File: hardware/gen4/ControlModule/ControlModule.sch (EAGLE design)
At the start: 43 parts, among them IC1 XMEGA16A4A

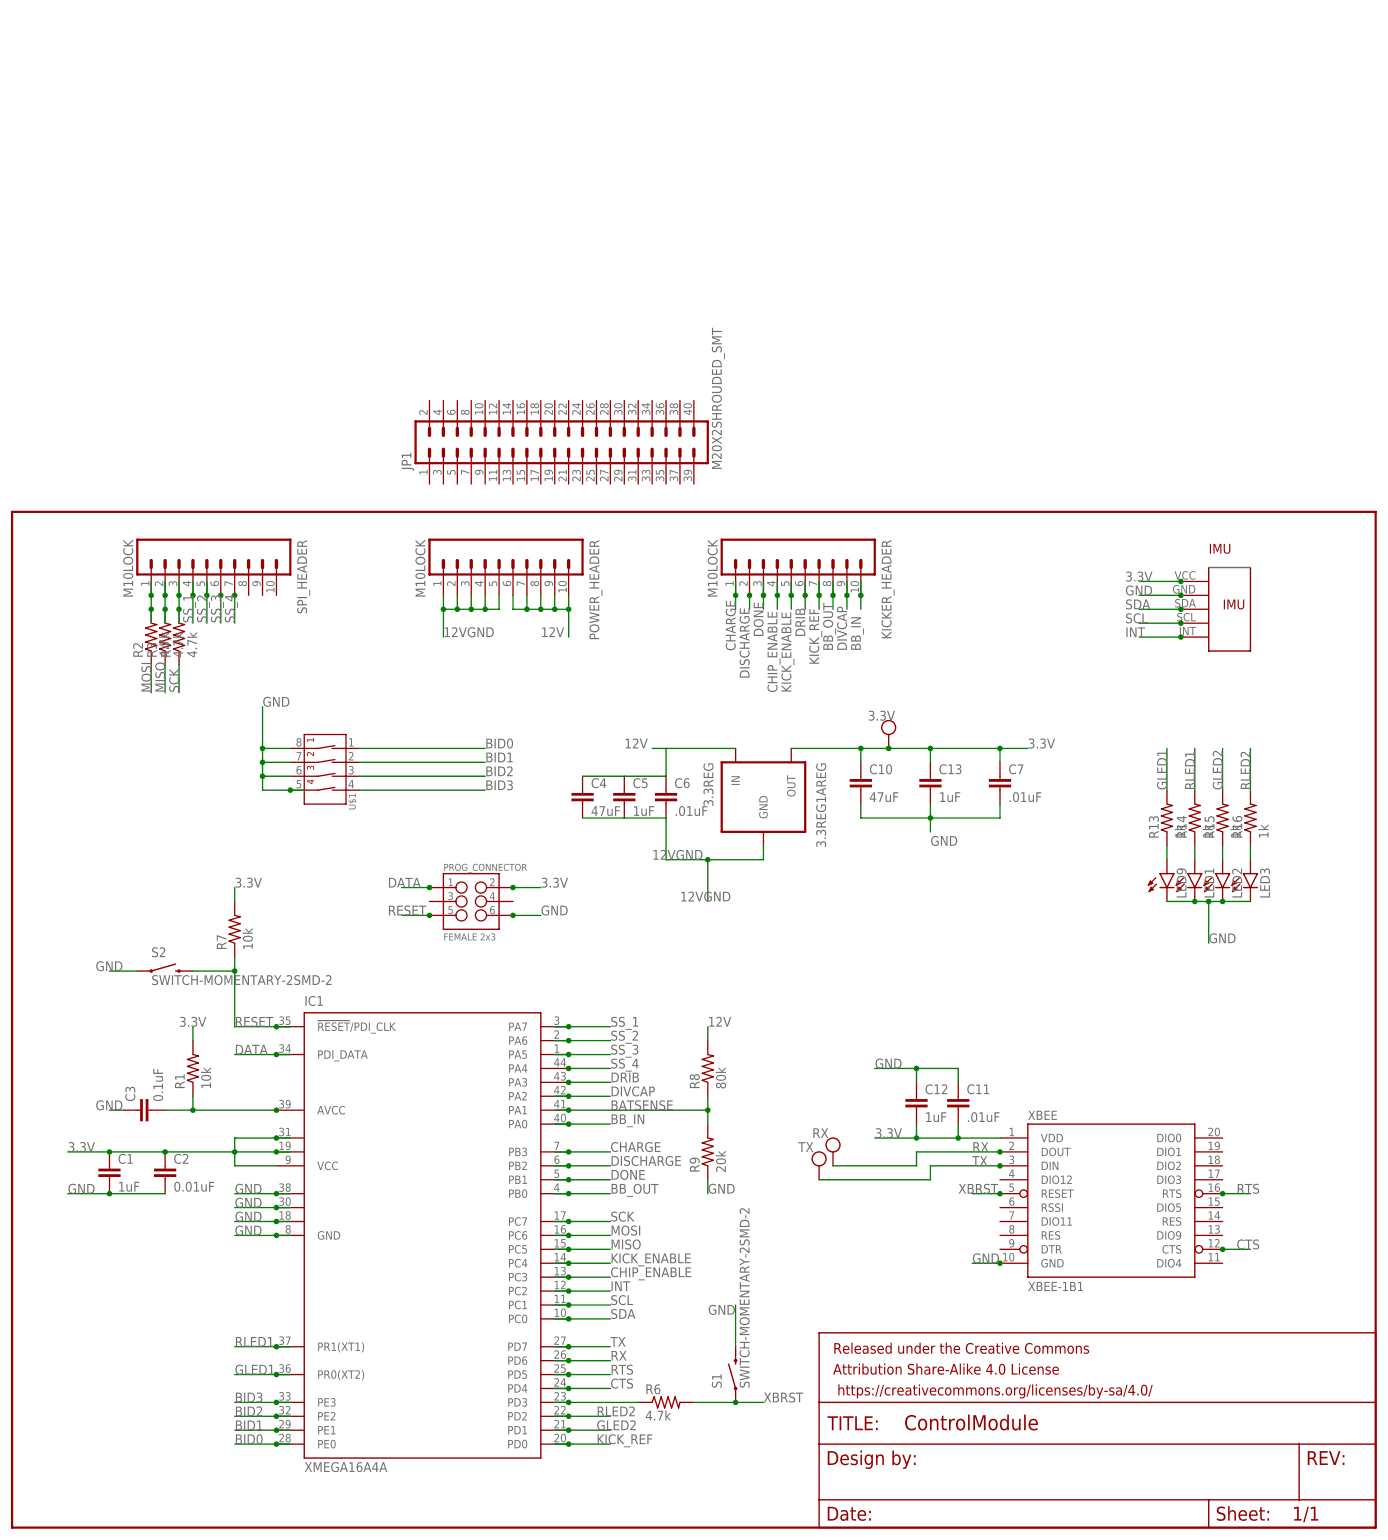
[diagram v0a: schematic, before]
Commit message: updated connectors
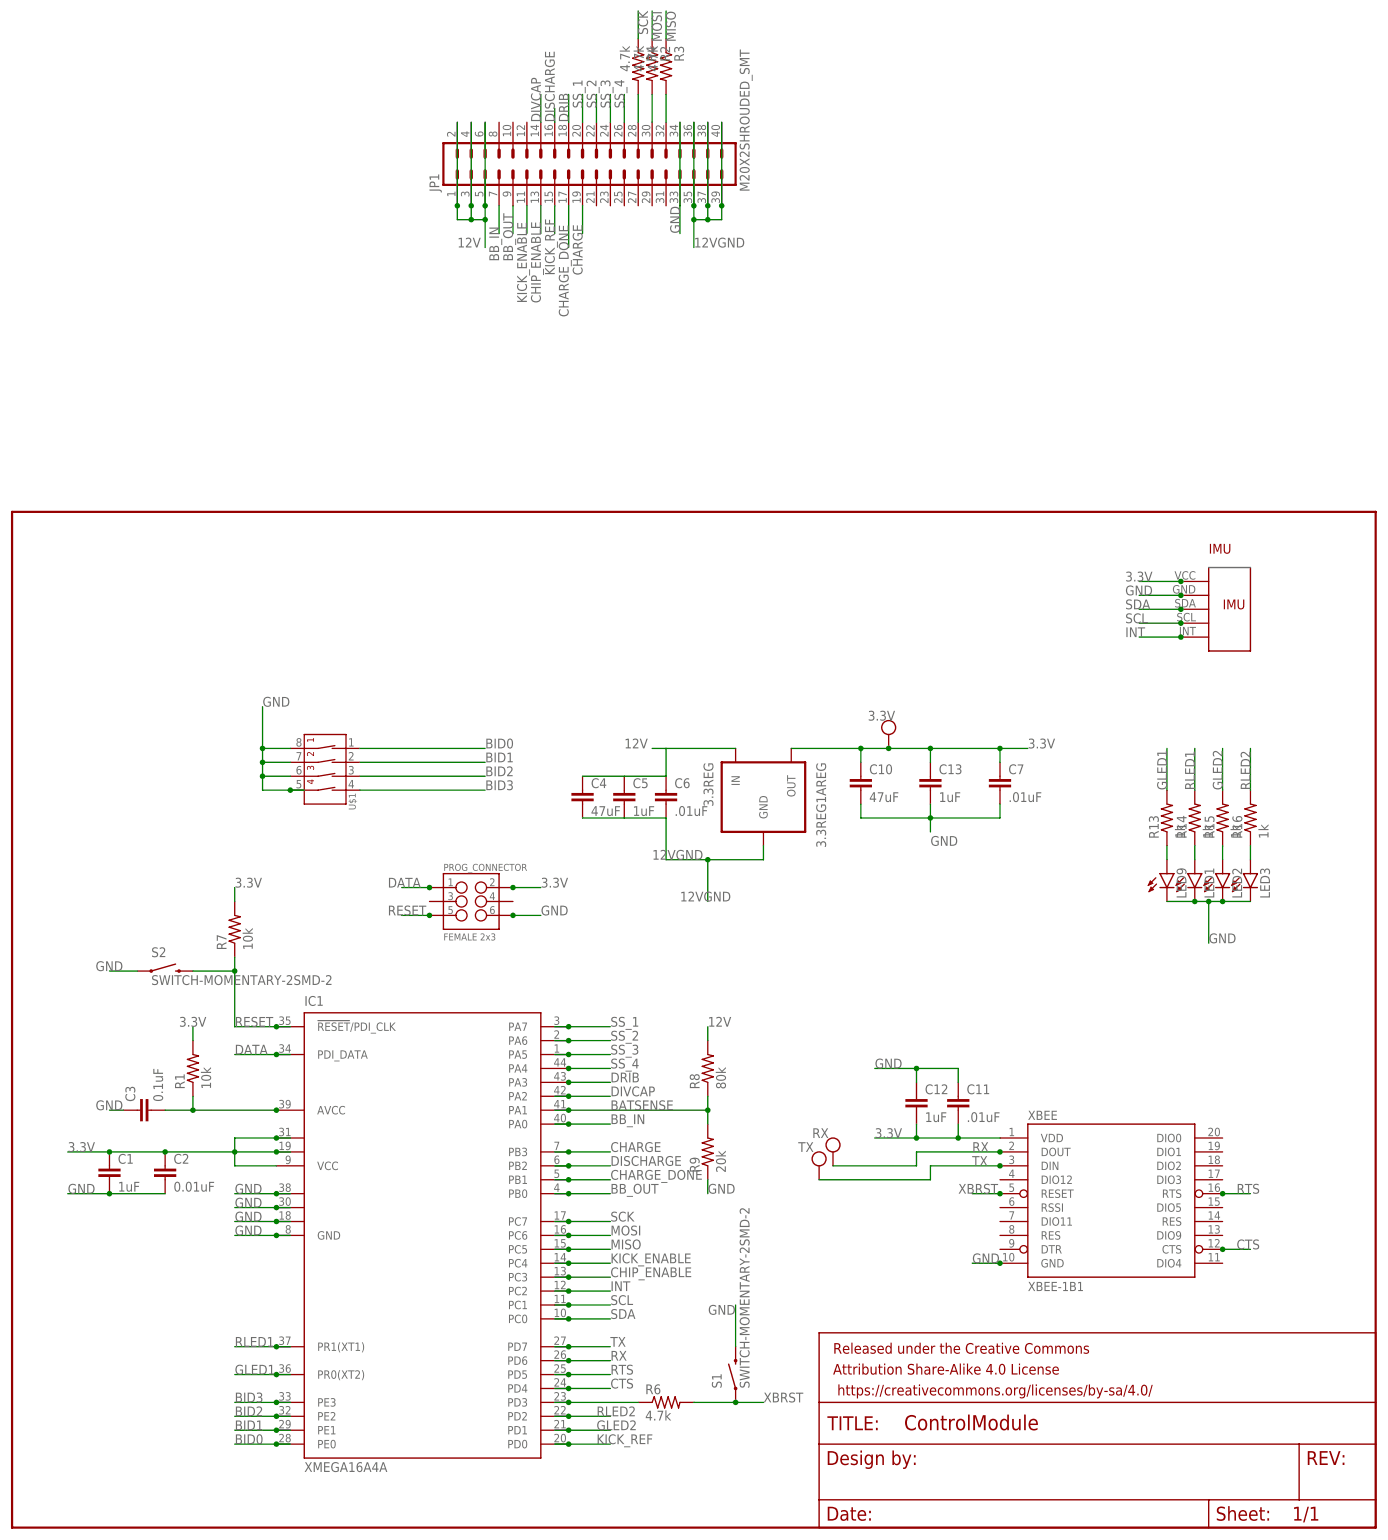
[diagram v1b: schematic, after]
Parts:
- removed KICKER_HEADER, POWER_HEADER, SPI_HEADER: M10LOCK, SparkFun-Connectors:M10LOCK
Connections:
- removed net DONE: IC1.PB1, KICKER_HEADER.3
- new net CHARGE_DONE: IC1.PB1
- net 12V: now also JP1.1, JP1.2, JP1.3, JP1.4, JP1.5, JP1.6; no longer POWER_HEADER.10, POWER_HEADER.6, POWER_HEADER.7, POWER_HEADER.8, POWER_HEADER.9
- net 12VGND: now also JP1.35, JP1.36, JP1.37, JP1.38, JP1.39, JP1.40; no longer POWER_HEADER.1, POWER_HEADER.2, POWER_HEADER.3, POWER_HEADER.4, POWER_HEADER.5
- net BB_IN: no longer KICKER_HEADER.10
- net BB_OUT: no longer KICKER_HEADER.8
- net CHARGE: no longer KICKER_HEADER.1
- net CHIP_ENABLE: no longer KICKER_HEADER.4
- net DISCHARGE: no longer KICKER_HEADER.2
- net DIVCAP: no longer KICKER_HEADER.9
- net DRIB: no longer KICKER_HEADER.6
- net GND: now also JP1.33, JP1.34
- net KICK_ENABLE: no longer KICKER_HEADER.5
- net KICK_REF: no longer KICKER_HEADER.7
- net N$6: no longer SPI_HEADER.1
- net N$7: no longer SPI_HEADER.2
- net N$8: no longer SPI_HEADER.3
- net SS_1: no longer SPI_HEADER.4
- net SS_2: no longer SPI_HEADER.5
- net SS_3: no longer SPI_HEADER.6
- net SS_4: no longer SPI_HEADER.7
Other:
- moved on the sheet: JP1, R2, R3, R4

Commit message: added new discharge circuit - spruced up for design review
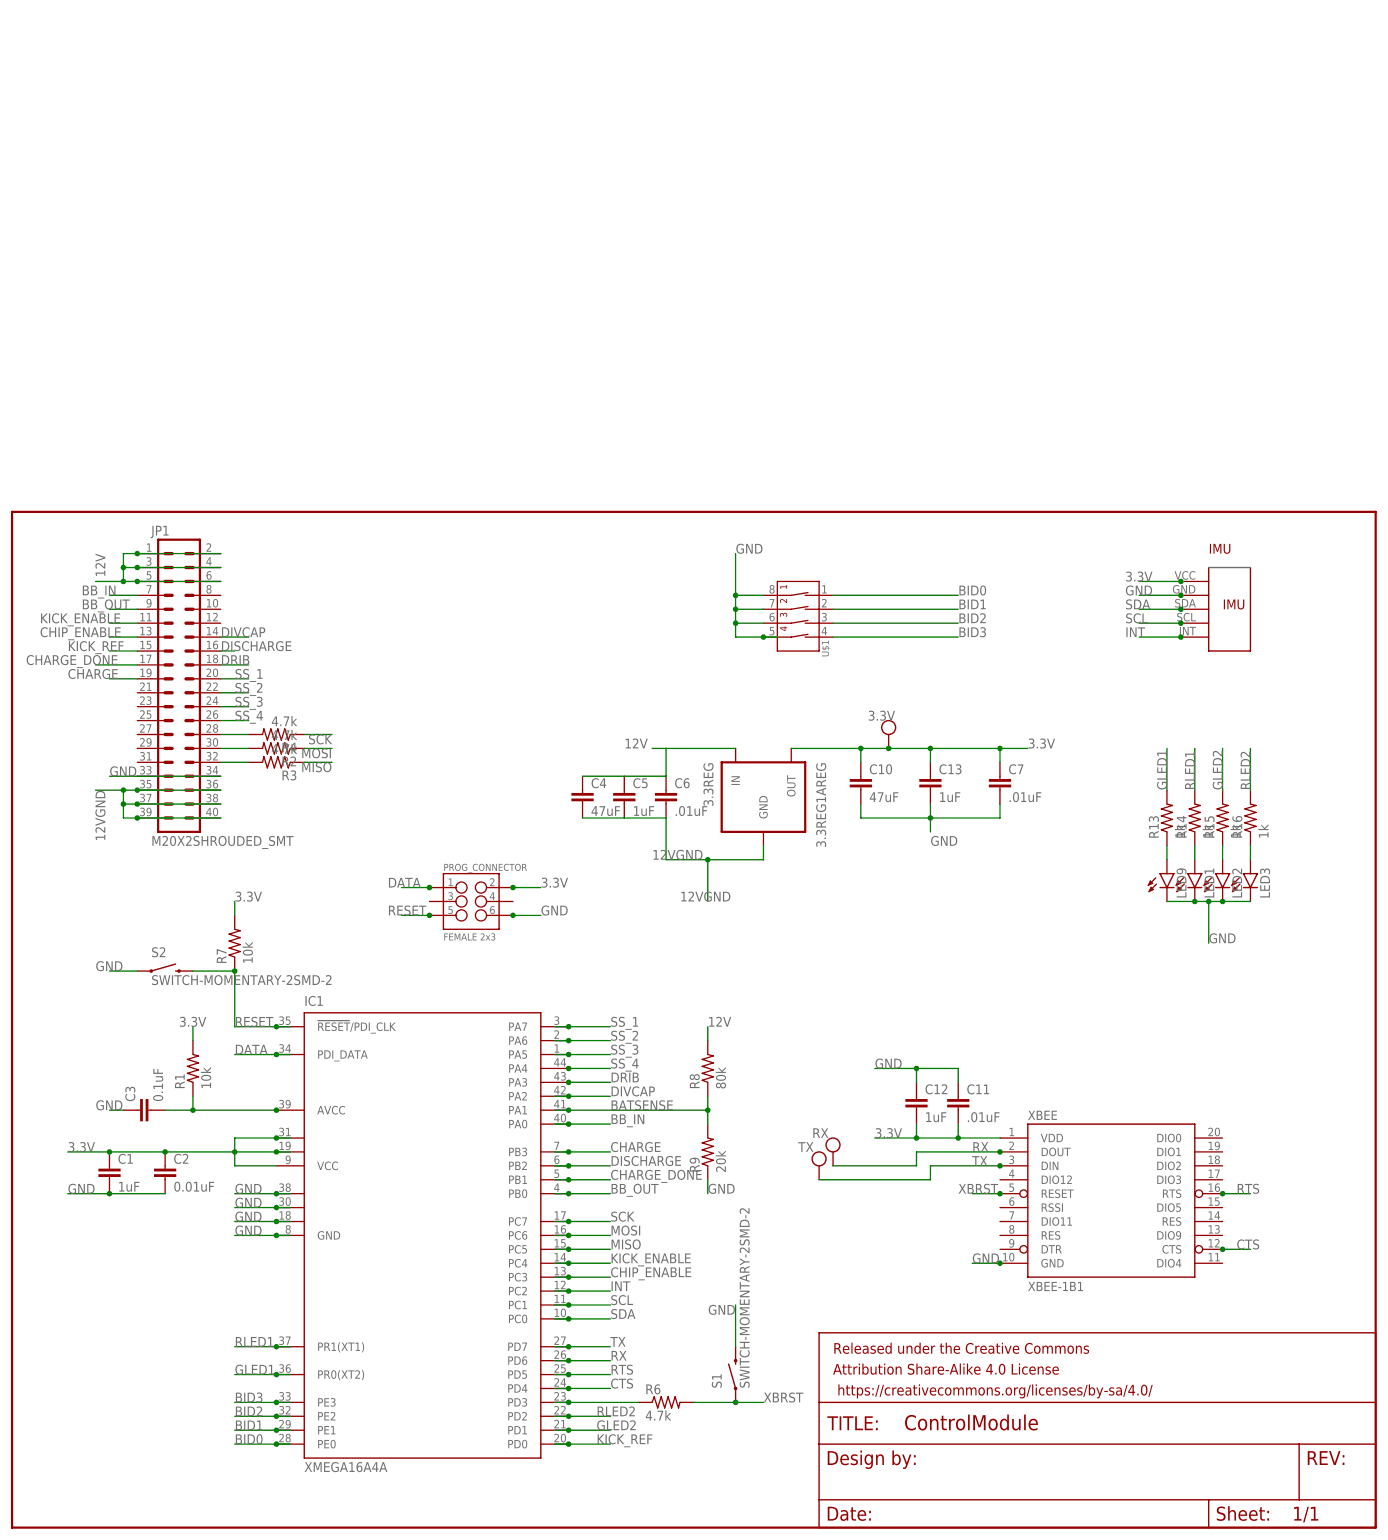
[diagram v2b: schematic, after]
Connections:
- net BB_IN: now also JP1.7
- net BB_OUT: now also JP1.9
- net CHARGE: now also JP1.19
- net CHARGE_DONE: now also JP1.17
- net CHIP_ENABLE: now also JP1.13
- net DISCHARGE: now also JP1.16
- net DIVCAP: now also JP1.14
- net DRIB: now also JP1.18
- net KICK_ENABLE: now also JP1.11
- net KICK_REF: now also JP1.15
- net N$6: now also JP1.30
- net N$7: now also JP1.32
- net N$8: now also JP1.28
- net SS_1: now also JP1.20
- net SS_2: now also JP1.22
- net SS_3: now also JP1.24
- net SS_4: now also JP1.26
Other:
- moved on the sheet: JP1, R2, R3, R4, R7, U$1

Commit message: almost done with shrinking comms board but computer is at 2 percent and I dont have a charger :/
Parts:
- removed IMU: MPU6050IMUMPU, gen3:MPU6050IMUMPU
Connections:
- net 3.3V: no longer IMU.VCC
- net GND: no longer IMU.GND
- net INT: no longer IMU.INT
- net SCL: no longer IMU.SCL
- net SDA: no longer IMU.SDA
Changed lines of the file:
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@@
 <?xml version="1.0" encoding="utf-8"?>
 <!DOCTYPE eagle SYSTEM "eagle.dtd">
-<eagle version="7.2.0">
+<eagle version="7.4.0">
 <drawing>
 <settings>
@@
 <part name="LED2" library="SparkFun-LED" deviceset="LED" device="1206"/>
 <part name="LED3" library="SparkFun-LED" deviceset="LED" device="1206"/>
-<part name="IMU" library="gen3" deviceset="MPU6050IMU" device="MPU"/>
 <part name="PROG_CONNECTOR" library="SparkFun-Connectors" deviceset="M03X2" device="FEMALE" value="FEMALE 2x3"/>
 <part name="C4" library="SparkFun-Capacitors" deviceset="CAP" device="1206" value="47uF"/>
@@
 <instance part="LED2" gate="G$1" x="220.98" y="119.38"/>
 <instance part="LED3" gate="G$1" x="226.06" y="119.38"/>
-<instance part="IMU" gate="G$1" x="220.98" y="167.64"/>
 <instance part="PROG_CONNECTOR" gate="G$1" x="83.82" y="114.3"/>
 <instance part="C4" gate="G$1" x="104.14" y="132.08"/>
@@
 <label x="218.44" y="106.68" size="1.778" layer="95"/>
 <label x="17.78" y="137.16" size="1.778" layer="95"/>
-</segment>
-<segment>
-<pinref part="IMU" gate="G$1" pin="GND"/>
-<wire x1="213.36" y1="170.18" x2="205.74" y2="170.18" width="0.1524" layer="91"/>
-<label x="203.2" y="170.18" size="1.778" layer="95"/>
-<junction x="213.36" y="170.18"/>
 </segment>
 <segment>
@@
 </segment>
 <segment>
-<pinref part="IMU" gate="G$1" pin="VCC"/>
-<wire x1="213.36" y1="172.72" x2="205.74" y2="172.72" width="0.1524" layer="91"/>
-<label x="203.2" y="172.72" size="1.778" layer="95"/>
-<junction x="213.36" y="172.72"/>
-</segment>
-<segment>
 <pinref part="PROG_CONNECTOR" gate="G$1" pin="2"/>
 <wire x1="91.44" y1="116.84" x2="96.52" y2="116.84" width="0.1524" layer="91"/>
@@
 <segment>
 <wire x1="99.06" y1="40.64" x2="101.6" y2="40.64" width="0.1524" layer="91"/>
-<label x="109.22" y="40.64" size="1.778" layer="95"/>
 <pinref part="IC1" gate="G$1" pin="PC1"/>
-<junction x="101.6" y="40.64"/>
-<wire x1="101.6" y1="40.64" x2="109.22" y2="40.64" width="0.1524" layer="91"/>
-</segment>
-<segment>
-<pinref part="IMU" gate="G$1" pin="SCL"/>
-<wire x1="213.36" y1="165.1" x2="205.74" y2="165.1" width="0.1524" layer="91"/>
-<label x="203.2" y="165.1" size="1.778" layer="95"/>
-<junction x="213.36" y="165.1"/>
 </segment>
 </net>
@@
 <segment>
 <wire x1="99.06" y1="38.1" x2="101.6" y2="38.1" width="0.1524" layer="91"/>
-<label x="109.22" y="38.1" size="1.778" layer="95"/>
 <pinref part="IC1" gate="G$1" pin="PC0"/>
-<junction x="101.6" y="38.1"/>
-<wire x1="101.6" y1="38.1" x2="109.22" y2="38.1" width="0.1524" layer="91"/>
-</segment>
-<segment>
-<pinref part="IMU" gate="G$1" pin="SDA"/>
-<wire x1="213.36" y1="167.64" x2="205.74" y2="167.64" width="0.1524" layer="91"/>
-<label x="203.2" y="167.64" size="1.778" layer="95"/>
-<junction x="213.36" y="167.64"/>
 </segment>
 </net>
@@
 <segment>
 <wire x1="99.06" y1="43.18" x2="101.6" y2="43.18" width="0.1524" layer="91"/>
-<label x="109.22" y="43.18" size="1.778" layer="95"/>
 <pinref part="IC1" gate="G$1" pin="PC2"/>
-<junction x="101.6" y="43.18"/>
-<wire x1="101.6" y1="43.18" x2="109.22" y2="43.18" width="0.1524" layer="91"/>
-</segment>
-<segment>
-<pinref part="IMU" gate="G$1" pin="INT"/>
-<wire x1="213.36" y1="162.56" x2="205.74" y2="162.56" width="0.1524" layer="91"/>
-<label x="203.2" y="162.56" size="1.778" layer="95"/>
-<junction x="213.36" y="162.56"/>
-</segment>
-</net>
+</segment>
+</net>
